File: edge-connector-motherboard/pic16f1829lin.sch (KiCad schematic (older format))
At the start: 6 parts, among them P3 MOLEX-22-28-6050, U1 PIC16F1829LIN

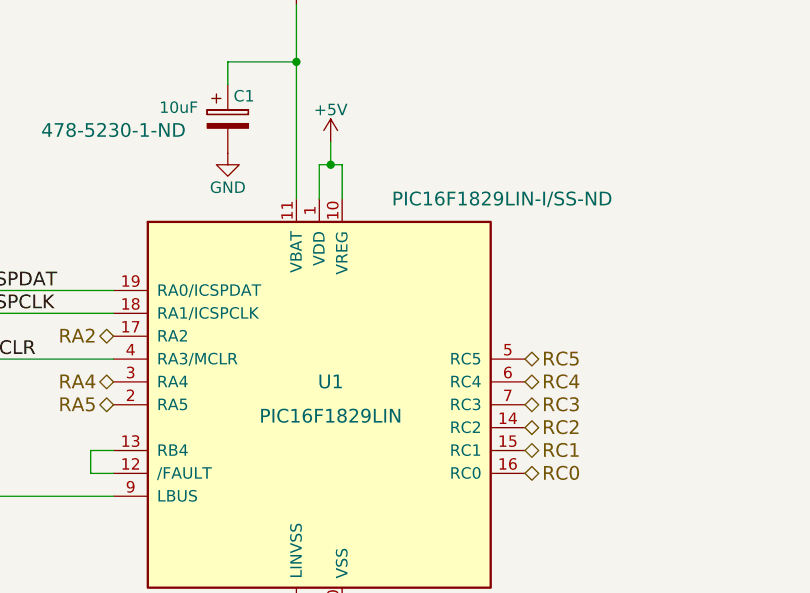
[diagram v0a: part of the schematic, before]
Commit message: edge-connector-motherboard: adding 3d models and digikey references
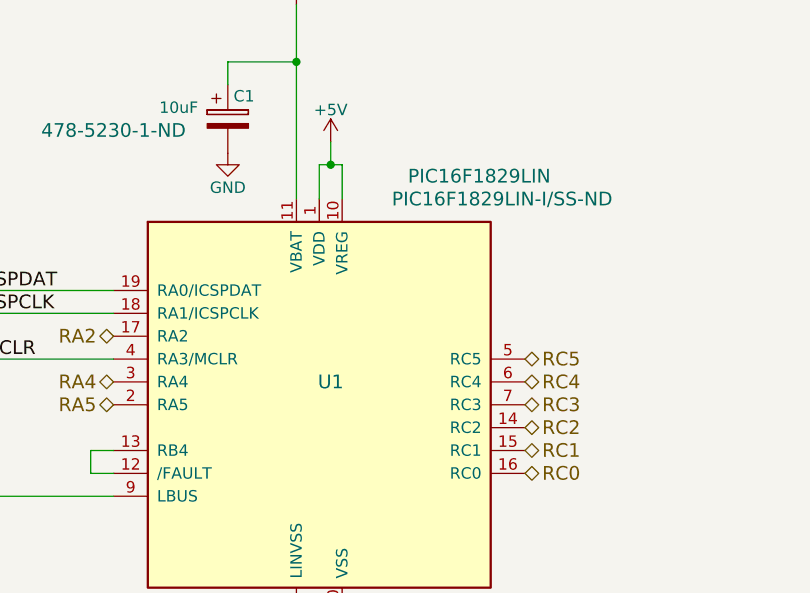
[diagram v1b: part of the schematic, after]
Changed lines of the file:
@@
 P 5950 4100
 F 0 "U1" H 6000 4200 60  0000 C CNN
-F 1 "PIC16F1829LIN" H 6000 4050 60  0000 C CNN
+F 1 "PIC16F1829LIN" H 6650 5100 60  0000 C CNN
 F 2 "Housings_SSOP:SSOP-20_5.3x7.2mm_Pitch0.65mm" H 5950 4100 60  0001 C CNN
 F 3 "http://ww1.microchip.com/downloads/en/DeviceDoc/41673A.pdf" H 5950 4100 60  0001 C CNN
